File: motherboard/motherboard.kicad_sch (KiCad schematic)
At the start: 1 part, among them J20 CM3588 Hirose Connector

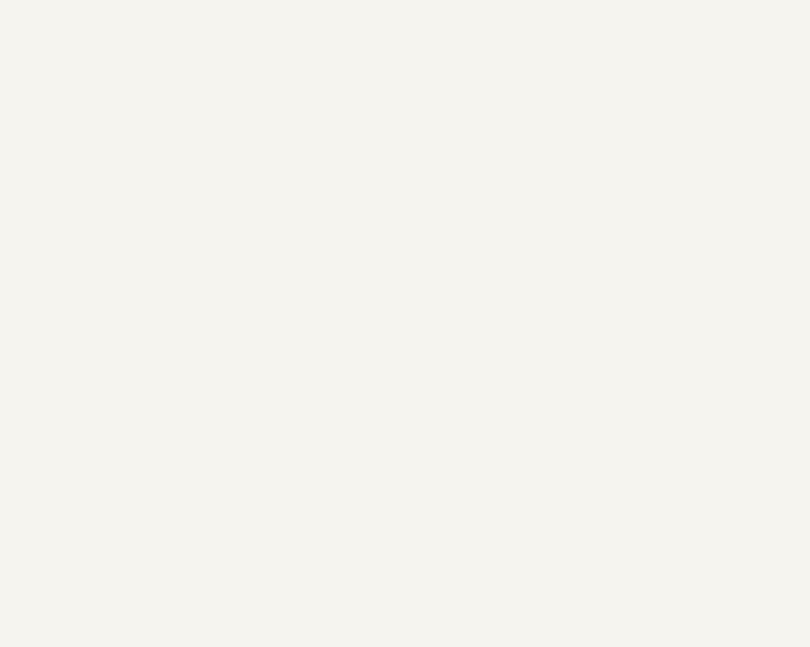
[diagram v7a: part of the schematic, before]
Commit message: uploaded cm3588 3d model, working on audio
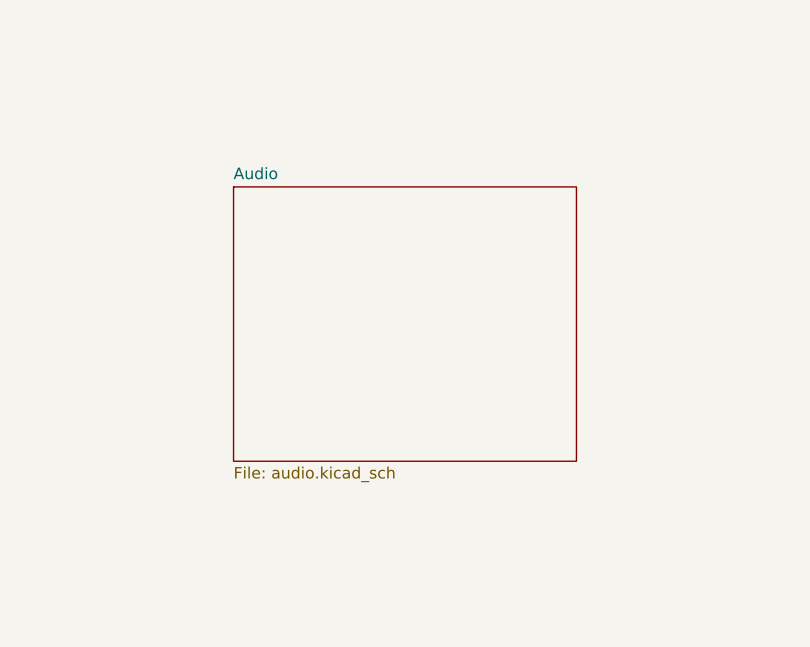
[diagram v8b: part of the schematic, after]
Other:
- added sheet Audio (audio.kicad_sch)
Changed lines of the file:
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@@
+	)
+	(sheet
+		(at 292.1 191.77)
+		(size 38.1 30.48)
+		(fields_autoplaced yes)
+		(stroke
+			(width 0.1524)
+			(type solid)
+		)
+		(fill
+			(color 0 0 0 0.0000)
+		)
+		(property "Sheetname" "Audio"
+			(at 292.1 191.0584 0)
+			(effects
+				(font
+					(size 1.27 1.27)
+				)
+				(justify left bottom)
+			)
+		)
+		(property "Sheetfile" "audio.kicad_sch"
+			(at 292.1 222.8346 0)
+			(effects
+				(font
+					(size 1.27 1.27)
+				)
+				(justify left top)
+			)
+		)
+		(instances
+			(project "motherboard"
+				(path "/025fe4d1-0305-4b34-be04-f8d9818125a4"
+					(page "12")
+				)
+			)
+		)
 	)
 	(sheet
